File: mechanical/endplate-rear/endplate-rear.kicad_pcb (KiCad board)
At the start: 2 copper layers, 88 x 38 mm, 0 parts

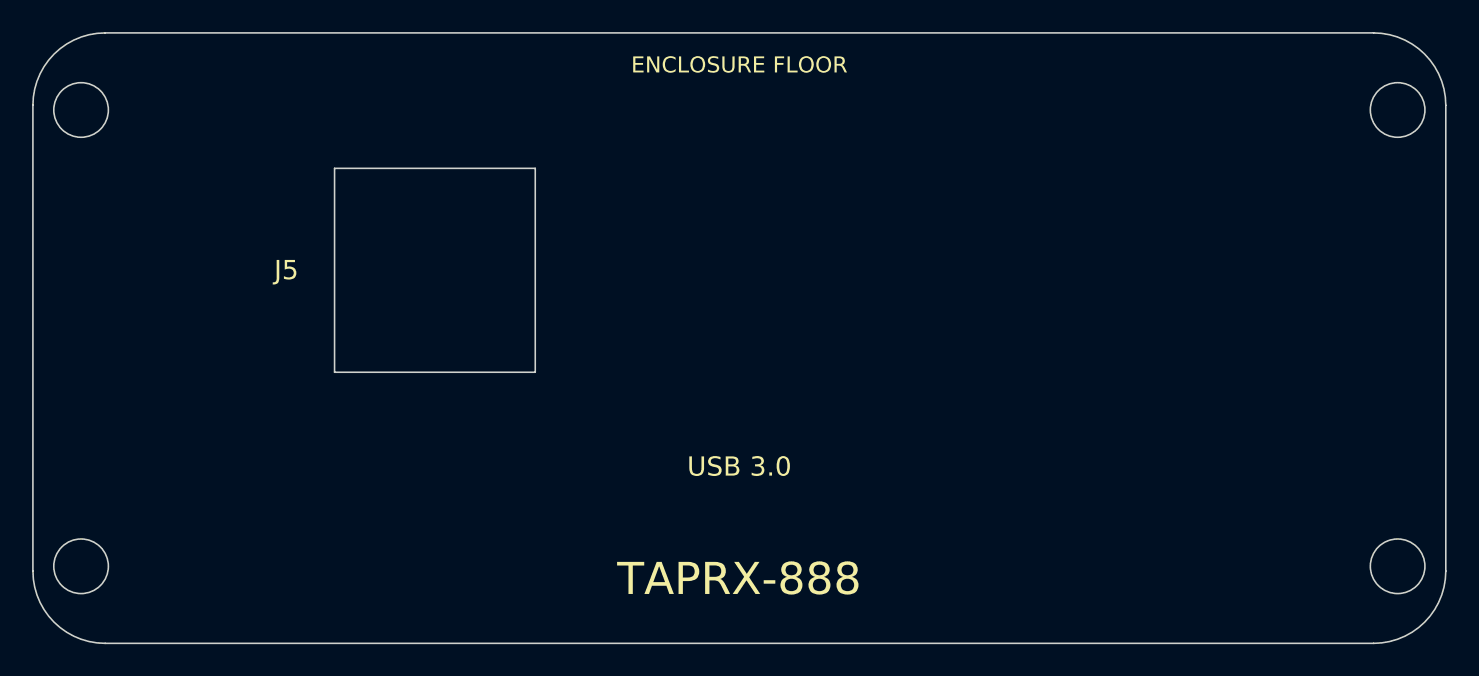
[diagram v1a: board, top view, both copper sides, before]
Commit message: mechanical: move connector labels to the floor side (exposed panel)
The interior side of each cutout is hidden behind the board once assembled, so
put the silkscreen on the floor side (toward the top edge): SMA function names
above their holes, USB label above its opening. Drop the per-hole J# from silk
(space is tight on the exposed strip) and record the J#->function map + floor
orientation in the Cmts.User note instead.

Co-Authored-By: Claude Opus 4.8 <noreply@anthropic.com>
Claude-Session: https://claude.ai/code/session_019A4jkTeNPLki8CdfTWEUwM
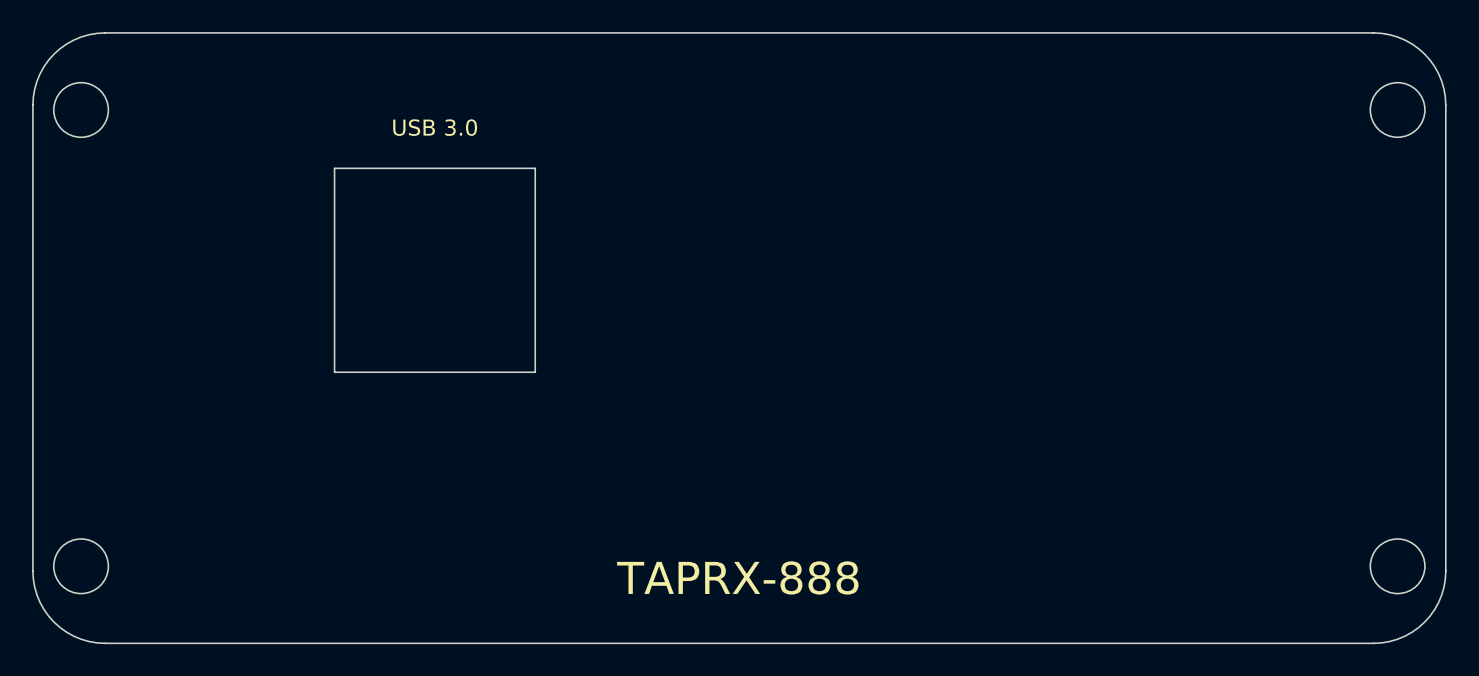
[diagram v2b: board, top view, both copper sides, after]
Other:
- board text added: "REAR PLATE: X mirrored vs front (outside view). Outline+M3 corner holes from enclosure DXF (88x38 R4.5, holes Ø3.4 @ +/-41,+/-14.21). Connector Y set from measured 7.9mm PCB rail height above enclosure floor (TOP edge, Y=0). SMA holes Ø7.0 at plate Y 7.90 (edge-launch, board plane). USB opening 12.5x12.7 at plate Y 14.79 (bottom flush to board top surface; connector rises 12.2 into box). Floor = 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"
- board text removed: "ENCLOSURE FLOOR"
- board text removed: "J5"
- board text removed: "REAR PLATE: X mirrored vs front (outside view). Outline+M3 corner holes from enclosure DXF (88x38 R4.5, holes Ø3.4 @ +/-41,+/-14.21). Connector Y set from measured 7.9mm PCB rail height above enclosure floor (TOP edge, Y=0). SMA holes Ø7.0 at plate Y 7.90 (edge-launch, board plane). USB opening 12.5x12.7 at plate Y 14.79 (bottom flush to board top surface; connector rises 12.2 into box). Open in 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"
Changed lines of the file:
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@@
 		(layer "Edge.Cuts")
 	)
-	(gr_text "J5"
-		(at 15.788 14.785)
-		(layer "F.SilkS")
-		(effects
-			(font
-				(size 1.2 1.2)
-				(thickness 0.2)
-			)
-		)
-	)
-	(gr_text "ENCLOSURE FLOOR"
-		(at 44.0 2)
+	(gr_text "USB 3.0"
+		(at 25.038 5.935)
 		(layer "F.SilkS")
 		(effects
@@
 				(size 1.0 1.0)
 				(thickness 0.15)
-			)
-		)
-	)
-	(gr_text "USB 3.0"
-		(at 44.0 27.02)
-		(layer "F.SilkS")
-		(effects
-			(font
-				(size 1.2 1.2)
-				(thickness 0.2)
 			)
 		)
@@
 		)
 	)
-	(gr_text "REAR PLATE: X mirrored vs front (outside view). Outline+M3 corner holes from enclosure DXF (88x38 R4.5, holes Ø3.4 @ +/-41,+/-14.21). Connector Y set from measured 7.9mm PCB rail height above enclosure floor (TOP edge, Y=0). SMA holes Ø7.0 at plate Y 7.90 (edge-launch, board plane). USB opening 12.5x12.7 at plate Y 14.79 (bottom flush to board top surface; connector rises 12.2 into box). Open in KiCad 10 to confirm parse."
+	(gr_text "REAR PLATE: X mirrored vs front (outside view). Outline+M3 corner holes from enclosure DXF (88x38 R4.5, holes Ø3.4 @ +/-41,+/-14.21). Connector Y set from measured 7.9mm PCB rail height above enclosure floor (TOP edge, Y=0). SMA holes Ø7.0 at plate Y 7.90 (edge-launch, board plane). USB opening 12.5x12.7 at plate Y 14.79 (bottom flush to board top surface; connector rises 12.2 into box). Floor = connector edge (top, Y=0). SMA: J1=RF IN J3=SPARE J2=TIMESYNC IN J4=EXT REF. Open in KiCad 10 to confirm parse."
 		(at 44.0 42.02)
 		(layer "Cmts.User")
